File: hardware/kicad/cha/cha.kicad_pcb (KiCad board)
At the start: 4 copper layers, 173 x 134 mm, 137 parts, among them J1 AES_CHA, J2 CONF C, J3 CONF SM, J4 microSD, J5 Câble PROG-CHA, SW1 Retour menu, U1 AMS1117-3.3, U10 74AHCT1G32, U11 74LVC1G07, U12 iCE40HX4K-TQ144, U13 AS4C32M16SB-6TIN, U14 iCE40HX4K-TQ144, U15 IS61WV10248EDBLL-10TLI, U2 AP2112K-1.2, U3 74LVC16244A, U4 74LVC16244A, U5 74LVC16244A, U6 74LVC16244A, U7 74AHCT16244, U8 74AHCT16244, U9 74AHCT244, X1 25 MHz 3,3 V, X2 25 MHz 3,3 V

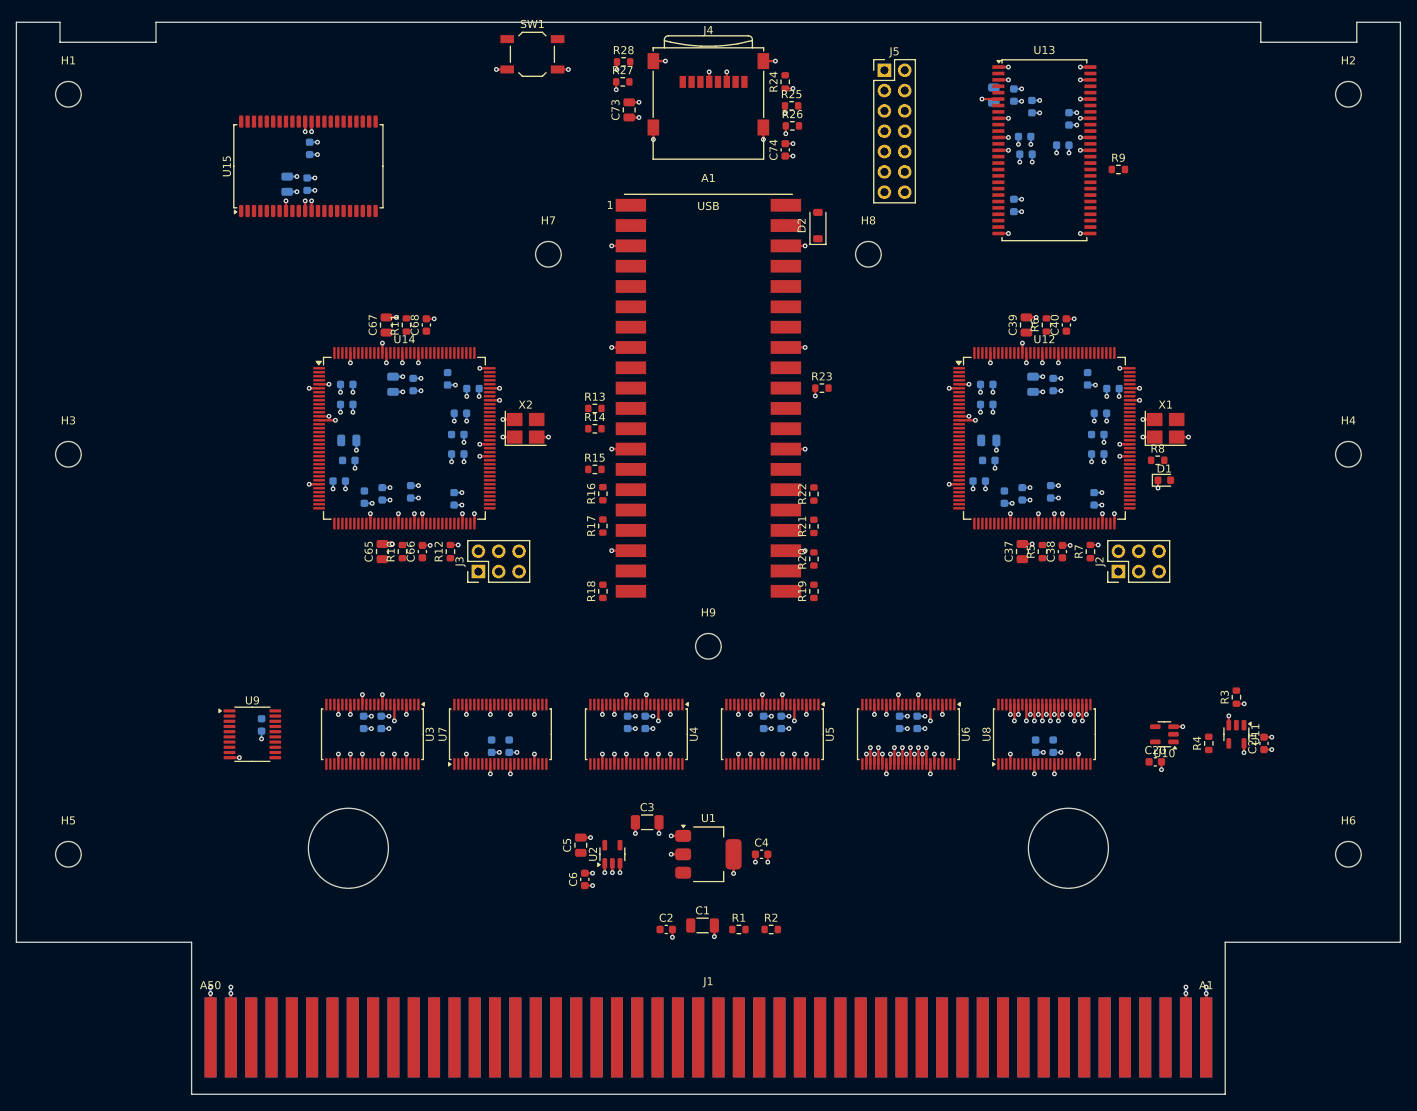
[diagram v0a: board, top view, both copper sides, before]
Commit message: Carte CHA entièrement routée
Après regroupement des canaux de U7 : routage Freerouting en 12 passes
puis raccordements aux plans, plus aucune liaison manquante. DRC :
aucune violation d'isolement ni court-circuit (restent sérigraphie et
bibliothèque non déclarée dans l'environnement). Les deux cartes sont
routées.

Co-Authored-By: Claude Opus 5.5 <noreply@anthropic.com>
Claude-Session: https://claude.ai/code/session_01WKfXP1YJ8otGxZ5dsY6Agh
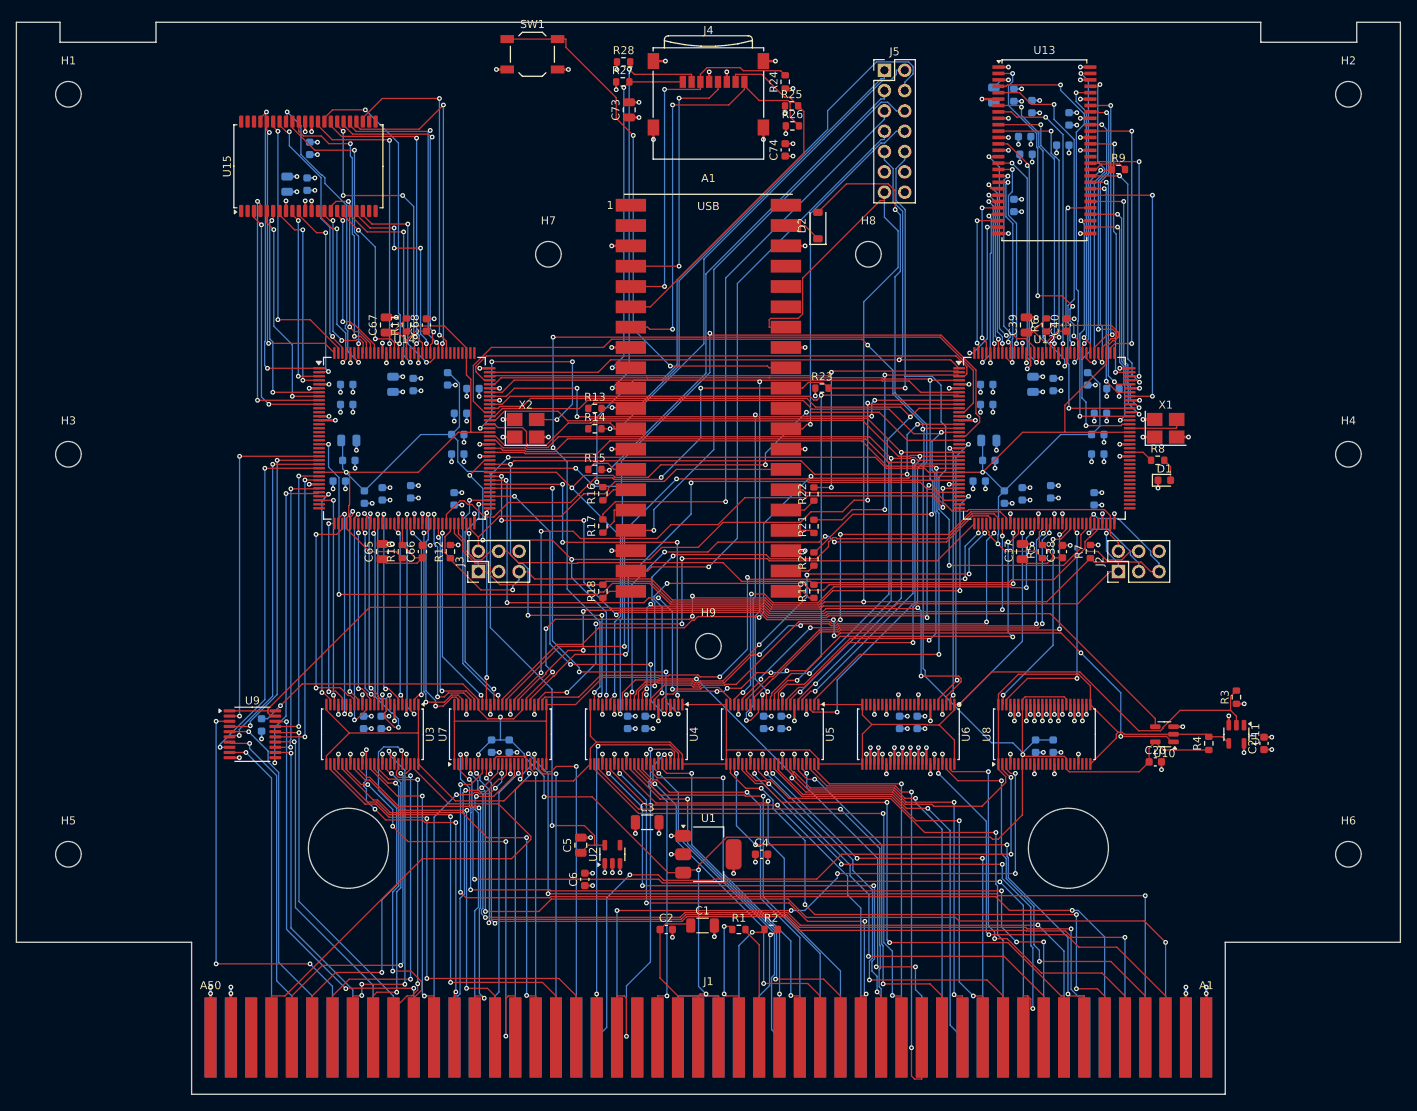
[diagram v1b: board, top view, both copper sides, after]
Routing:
- net +5V: track 0.00 -> 345.0 mm, vias 0 -> 9
- net +1V2: track 0.00 -> 310.5 mm, vias 0 -> 5
- net XLAT_EN_N: track 0.00 -> 210.9 mm, vias 0 -> 2
- net CRESET_N: track 0.00 -> 196.4 mm, vias 0 -> 3
- net CDONE: track 0.00 -> 150.9 mm, vias 0 -> 4
- net OE5_N: track 0.00 -> 144.9 mm, vias 0 -> 2
- net SDD_OE5_N: track 0.00 -> 129.5 mm
- net P4: track 0.00 -> 122.7 mm, vias 0 -> 3
- net AES_FIXD0: track 0.00 -> 119.4 mm, vias 0 -> 3
- net P10: track 0.00 -> 117.7 mm, vias 0 -> 3
- net P14: track 0.00 -> 116.2 mm, vias 0 -> 3
- net AES_FIXD1: track 0.00 -> 116.2 mm, vias 0 -> 3
- net AES_FIXD3: track 0.00 -> 113.4 mm, vias 0 -> 3
- net AES_FIXD2: track 0.00 -> 113.0 mm, vias 0 -> 3
- net PCK2B: track 0.00 -> 112.9 mm, vias 0 -> 4
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
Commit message: Pico 2, microSD et bouton sur la carte PROG ; pistes d'alimentation larges
- La carte PROG est côté avant de la cartouche, composants vers l'avant :
  lecteur microSD et bouton accessibles. Le câble PROG-CHA porte
  désormais le bus de liaison C/SM ; connecteur au même endroit sur les
  deux cartes (x = 172 mm), prêt pour un connecteur carte à carte.
- Sous le Pico : ni piste ni via sur la face composants (pastilles de
  test nues sous le module).
- Classes de réseaux écrites dans le .kicad_pro : +5V et VSYS en 0,5 mm,
  +1V2 en 0,3 mm.
- Broches des FPGA réoptimisées ; contrôle Freerouting sans violation ;
  routage des deux cartes et vérification de timing en cours.

Co-Authored-By: Claude Opus 5.5 <noreply@anthropic.com>
Claude-Session: https://claude.ai/code/session_01WKfXP1YJ8otGxZ5dsY6Agh
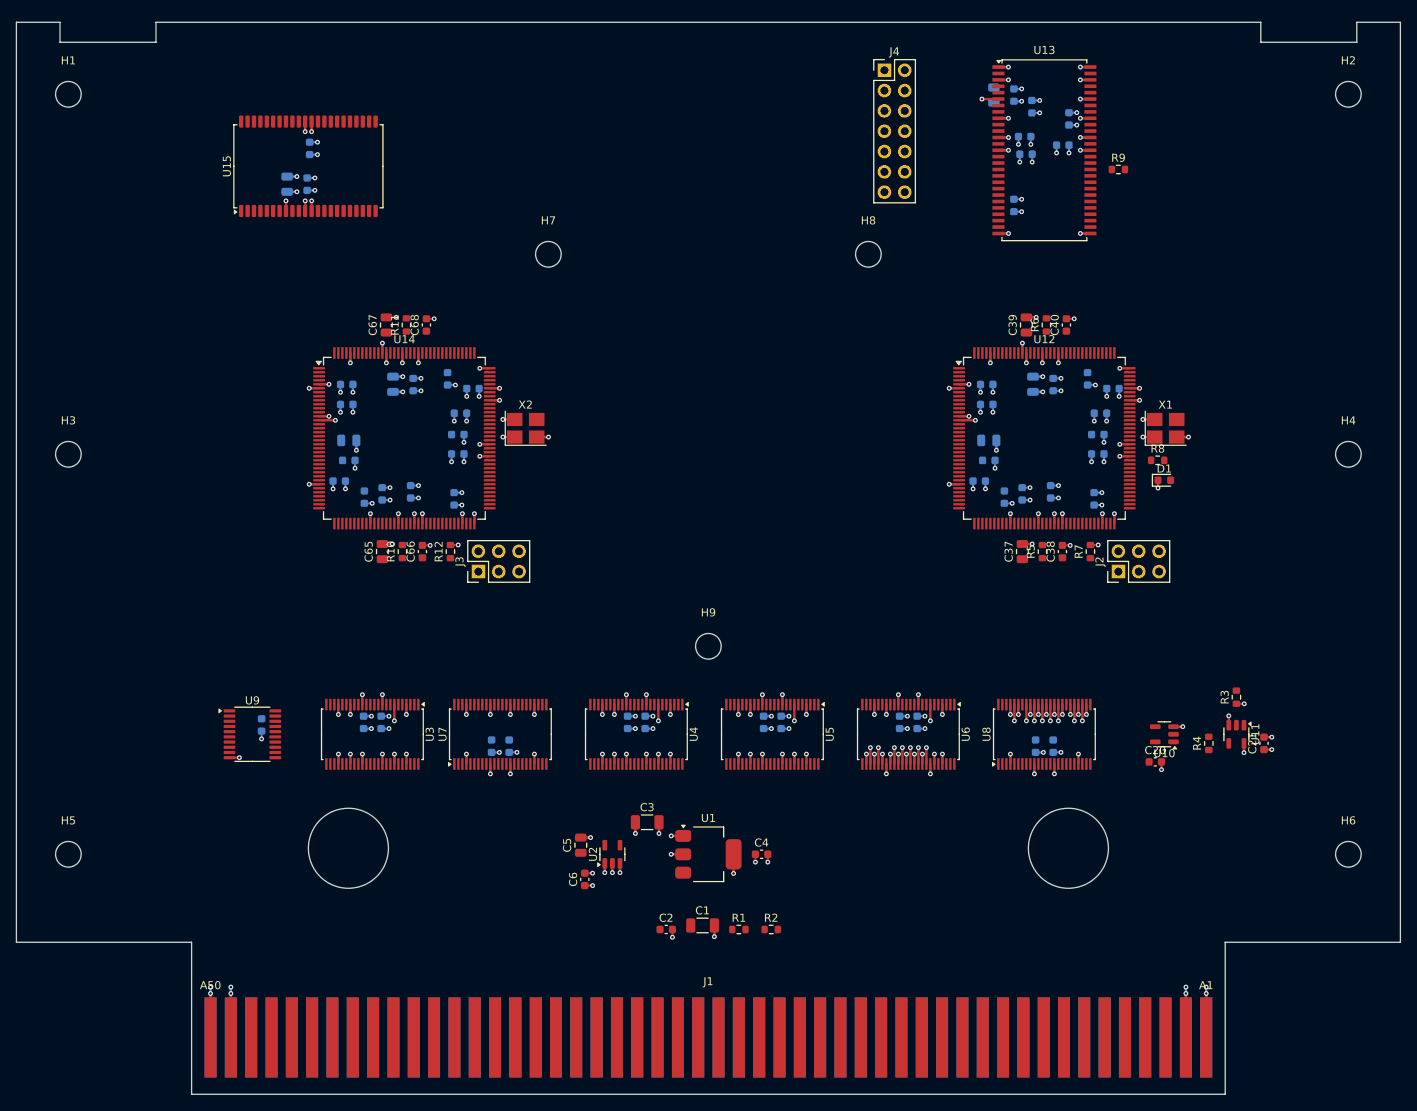
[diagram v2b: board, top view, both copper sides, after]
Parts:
- removed A1: Raspberry Pi Pico 2, SDAES:RaspberryPi_Pico2_SMD
- removed C73: 10u, Capacitor_SMD:C_0805_2012Metric
- removed C74: 100n, Capacitor_SMD:C_0603_1608Metric
- removed D2: SS14 / BAT60A, Diode_SMD:D_SOD-123
- removed J5: Câble PROG-CHA, Connector_PinHeader_2.54mm:PinHeader_2x07_P2.54mm_Vertical
- removed R13, R14, R15, R16, R17, R18, R19, R20, R21, R22: 33, Resistor_SMD:R_0603_1608Metric
- removed R23, R24, R25, R26, R27, R28: 10k, Resistor_SMD:R_0603_1608Metric
- removed SW1: Retour menu, Button_Switch_SMD:SW_SPST_TL3342
- J4: value microSD -> Câble PROG-CHA; footprint Connector_Card:microSD_HC_Wuerth_693072010801 -> Connector_PinHeader_2.54mm:PinHeader_2x07_P2.54mm_Vertical
- moved J4 22.2 mm to (172.0, 52.0)
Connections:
- J4 pad 1: SD_D2 -> CHA_SCK
- J4 pad 2: SD_D3 -> CHA_IO0
- J4 pad 3: SD_CMD -> CHA_IO1
- J4 pad 4: +3V3 -> CHA_IO2
- J4 pad 5: SD_CLK -> CHA_IO3
- J4 pad 6: GND -> CS_C
- J4 pad 7: SD_D0 -> CS_SM
- J4 pad 8: SD_D1 -> GND
- J4 pad 9: GND -> MODE
- U12 pad 1: MODE -> CHA_IO2
- U12 pad 10: P12 -> P2
- U12 pad 12: P10 -> P12
- U12 pad 2: CHA_IO3 -> CHA_IO1
- U12 pad 3: CHA_IO2 -> CHA_IO3
- U12 pad 4: CHA_IO1 -> MODE
- U12 pad 8: P2 -> P1
- U12 pad 9: P1 -> P10
- U14 pad 101: P1 -> P2
- U14 pad 104: CHA_IO1 -> MODE
- U14 pad 105: CHA_IO2 -> CHA_IO3
- U14 pad 106: CHA_IO3 -> CHA_IO2
- U14 pad 107: MODE -> CHA_IO1
- U14 pad 85: P12 -> P10
- U14 pad 88: P9 -> P12
- U14 pad 90: P10 -> P9
- U14 pad 99: P2 -> P1
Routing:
- net +5V: track 345.0 -> 0.00 mm, vias 9 -> 0
- net +1V2: track 310.5 -> 0.00 mm, vias 5 -> 0
- net XLAT_EN_N: track 210.9 -> 0.00 mm, vias 2 -> 0
- net CRESET_N: track 196.4 -> 0.00 mm, vias 3 -> 0
- net CDONE: track 150.9 -> 0.00 mm, vias 4 -> 0
- net OE5_N: track 144.9 -> 0.00 mm, vias 2 -> 0
- net SDD_OE5_N: track 129.5 -> 0.00 mm
- net P4: track 122.7 -> 0.00 mm, vias 3 -> 0
- net AES_FIXD0: track 119.4 -> 0.00 mm, vias 3 -> 0
- net P10: track 117.7 -> 0.00 mm, vias 3 -> 0
- net P14: track 116.2 -> 0.00 mm, vias 3 -> 0
- net AES_FIXD1: track 116.2 -> 0.00 mm, vias 3 -> 0
- net AES_FIXD3: track 113.4 -> 0.00 mm, vias 3 -> 0
- net AES_FIXD2: track 113.0 -> 0.00 mm, vias 3 -> 0
- net PCK2B: track 112.9 -> 0.00 mm, vias 4 -> 0
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
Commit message: Carte CHA : une seule liaison restante (+5V de U8, broche 31)
Routeur de finition (grille 0,05 mm, pistes de 0,1 mm, marge 0,03) :
CRESET_N et C_SD_DQ7 reliés, aucune violation de cuivre.

Co-Authored-By: Claude Opus 5.5 <noreply@anthropic.com>
Claude-Session: https://claude.ai/code/session_01WKfXP1YJ8otGxZ5dsY6Agh
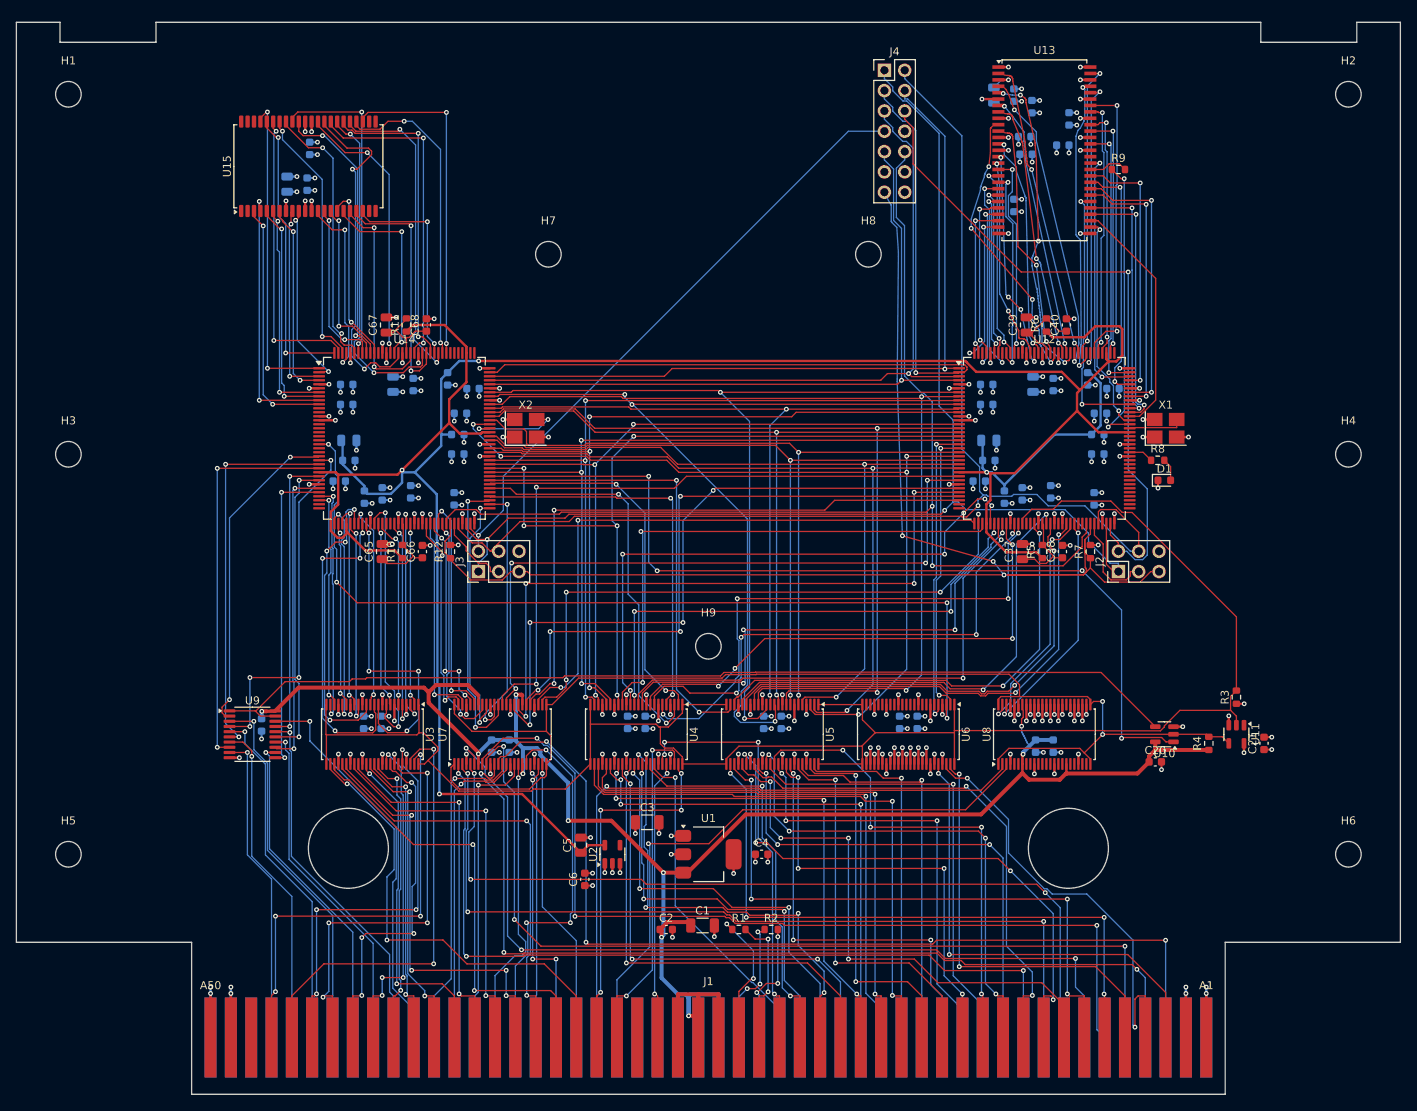
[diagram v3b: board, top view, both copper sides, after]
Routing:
- net +1V2: track 0.00 -> 338.8 mm, vias 0 -> 4
- net +5V: track 0.00 -> 249.0 mm, vias 0 -> 10
- net XLAT_EN_N: track 0.00 -> 230.4 mm
- net CRESET_N: track 0.00 -> 174.1 mm, vias 0 -> 3
- net CHA_IO0: track 0.00 -> 161.7 mm, vias 0 -> 1
- net CHA_SCK: track 0.00 -> 158.7 mm, vias 0 -> 2
- net OE5_N: track 0.00 -> 153.2 mm, vias 0 -> 2
- net CDONE: track 0.00 -> 139.5 mm, vias 0 -> 2
- net SDD_OE5_N: track 0.00 -> 123.3 mm
- net AES_FIXD0: track 0.00 -> 119.6 mm, vias 0 -> 3
- net P1: track 0.00 -> 117.1 mm, vias 0 -> 2
- net AES_FIXD1: track 0.00 -> 116.1 mm, vias 0 -> 3
- net SDD_OE_N: track 0.00 -> 115.0 mm, vias 0 -> 4
- net AES_FIXD2: track 0.00 -> 114.8 mm, vias 0 -> 3
- net AES_FIXD3: track 0.00 -> 113.1 mm, vias 0 -> 3
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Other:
- board text added: "Contacts de bord : or dur, biseau 45° (chanfrein). Finition ENIG, 4 couches, 1,6 mm."
